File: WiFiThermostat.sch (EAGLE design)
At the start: 1 part

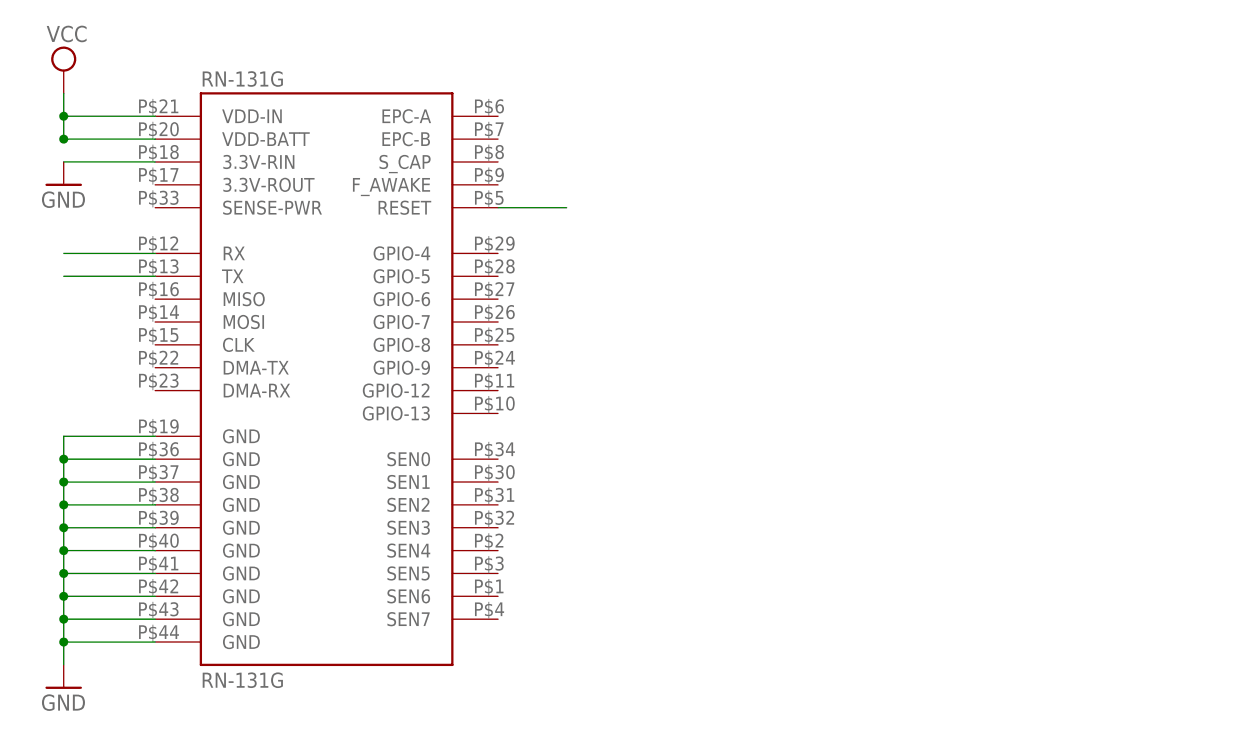
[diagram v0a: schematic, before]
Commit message: Added MSP430 and updated WiFly to have correct pin names
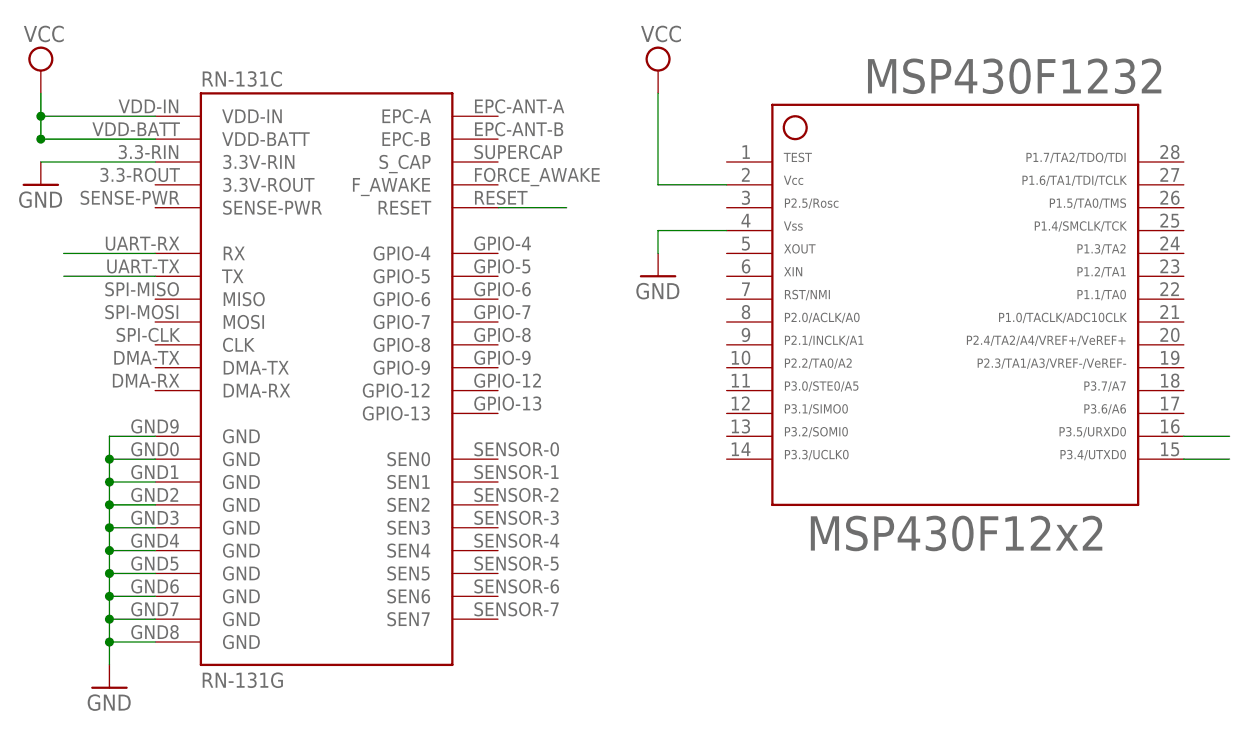
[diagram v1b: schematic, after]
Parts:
- added MSP430F1232: F12X2---DW28, TI_MSP430_v16:F12X2---DW28
- renumbered RN-131G to RN-131C
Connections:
- removed net RX: RN-131C.RX
- removed net TX: RN-131C.TX
- new net RN-RX: MSP430F1232.15, RN-131C.RX
- new net RN-TX: MSP430F1232.16, RN-131C.TX
- net GND: now also MSP430F1232.4
- net VCC: now also MSP430F1232.2
